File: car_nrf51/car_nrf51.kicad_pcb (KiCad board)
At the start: 2 copper layers, 56.5 x 60.3 mm, 28 parts, among them P1 CONN_02X10, P2 nrf51-breakout, P3 CONN_02X04, Q1 BC850, U1 DRIVER-TB6612FNG-O/C8/EL(SSOP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, U3 LM317_SOT223

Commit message: Fix motor driver footprint.
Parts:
- U1: footprint Housings_SSOP:SSOP-24_3.9x8.7mm_Pitch0.635mm -> Housings_SSOP:SSOP-24_5.3x8.2mm_Pitch0.65mm
- moved U1 1.54 mm to (146.4, 82.3)
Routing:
- net GND: track 213.5 -> 218.5 mm
- net /Motor2-: track 25.3 -> 29.8 mm
- net /Motor2+: track 19.5 -> 22.5 mm
- net /Motor1-: track 14.8 -> 17.2 mm
- net /Motor1+: track 8.35 -> 9.19 mm

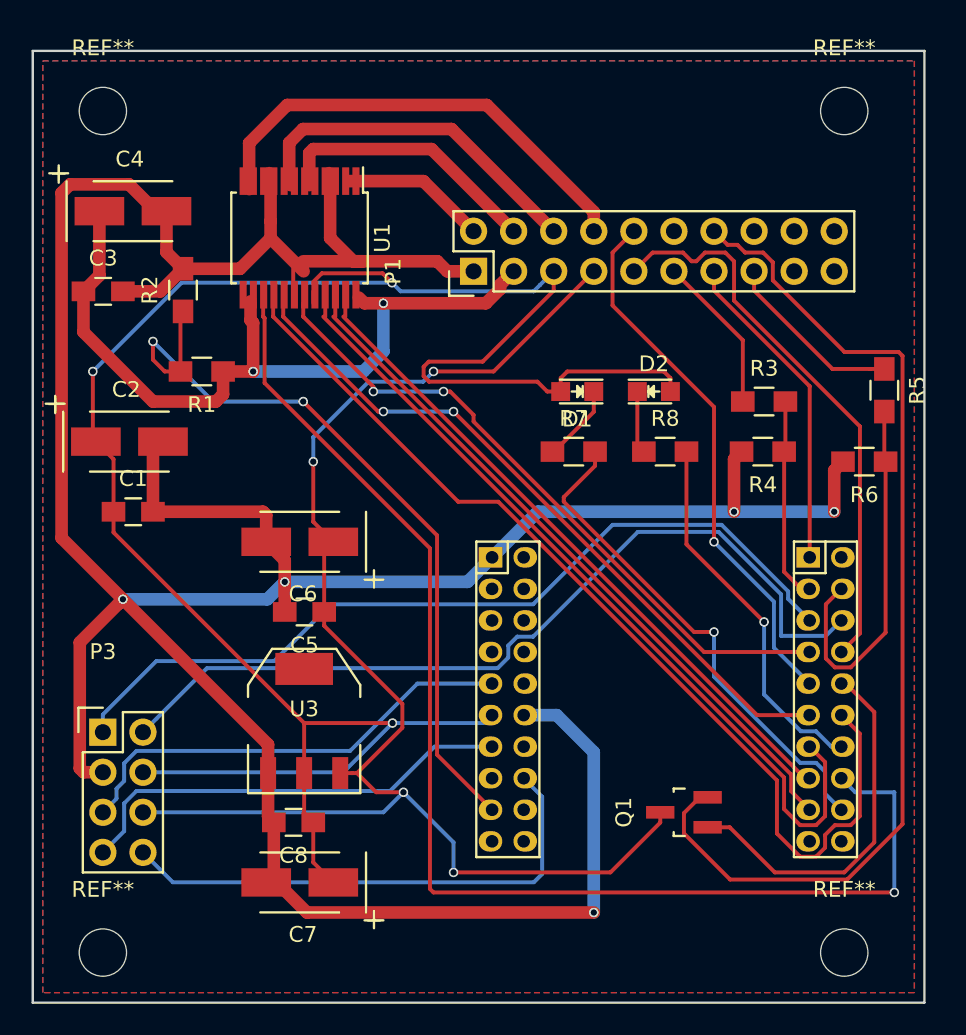
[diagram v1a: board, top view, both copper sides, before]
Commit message: Increase via pad size to 0.9mm.
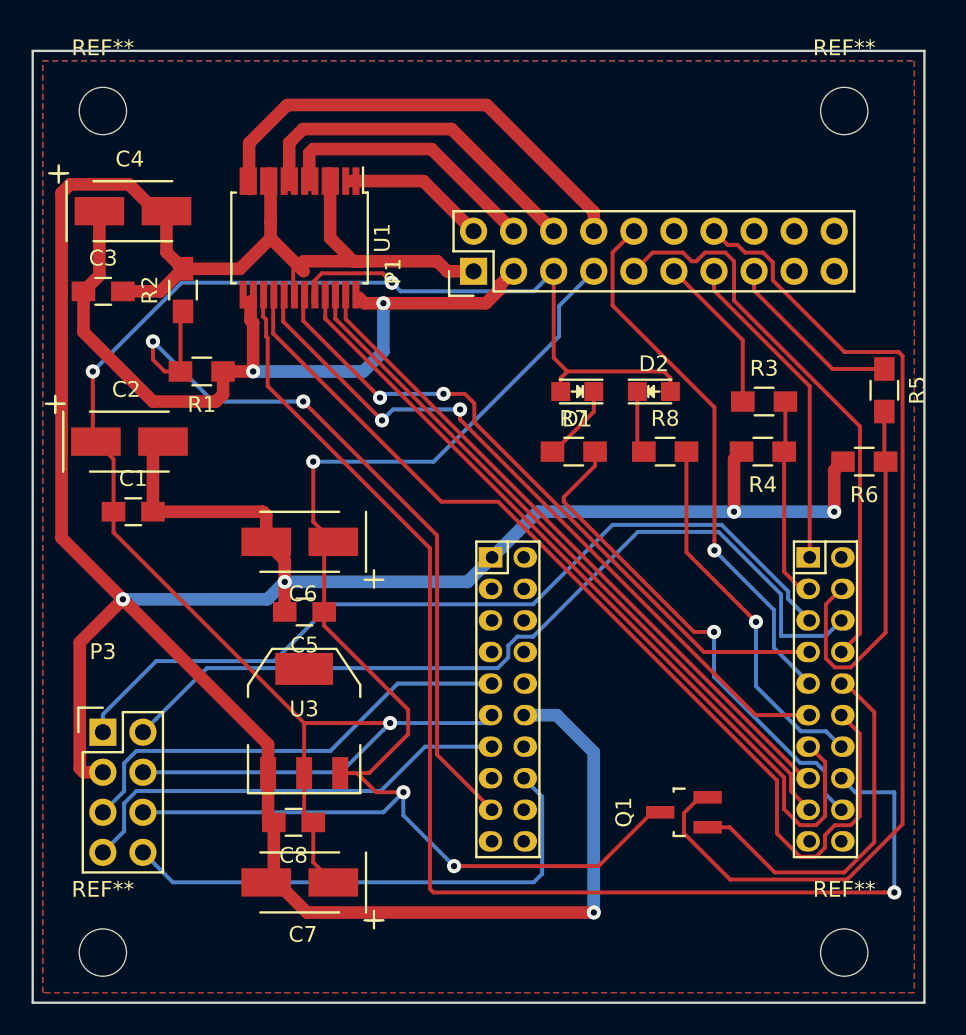
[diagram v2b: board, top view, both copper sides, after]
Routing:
- net +3V3: track 136.6 -> 122.0 mm
- net /AIN1: track 52.2 -> 54.2 mm
- net /BIN1: track 44.7 -> 45.8 mm
- net /PWMA: track 42.5 -> 43.3 mm
- net /STBY: track 42.2 -> 42.8 mm
- net /BIN2: track 62.6 -> 63.2 mm
- net +5V: vias 4 -> 3

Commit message: Send to pcb service.
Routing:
- net /PWMB: track 81.1 -> 79.7 mm
- net GND: track 218.5 -> 219.8 mm
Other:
- net class Default: clearance 0.2 -> 0.25; via_dia 0.6 -> 0.9; via_drill 0.4 -> 0.5
- net class Motor: clearance 0.2 -> 0.25; via_dia 0.6 -> 0.9; via_drill 0.4 -> 0.5
- rule trace_clearance: 0.2 -> 0.25
- rule trace_min: 0.2 -> 0.25
- rule via_min_size: 0.4 -> 0.9
